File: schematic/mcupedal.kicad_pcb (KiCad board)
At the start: 2 copper layers, 33 x 87.6 mm, 23 parts, among them J1 Barrel_Jack_Switch, J2 AudioJack3_Switch, J3 Screw_Terminal_01x02, J4 AudioJack3_Switch, J5 Screw_Terminal_01x03, J6 Screw_Terminal_01x03, U1 AMS1117-3.3, U2 footswitch, U3 Opamp_Dual, U4 ATtiny85-20P

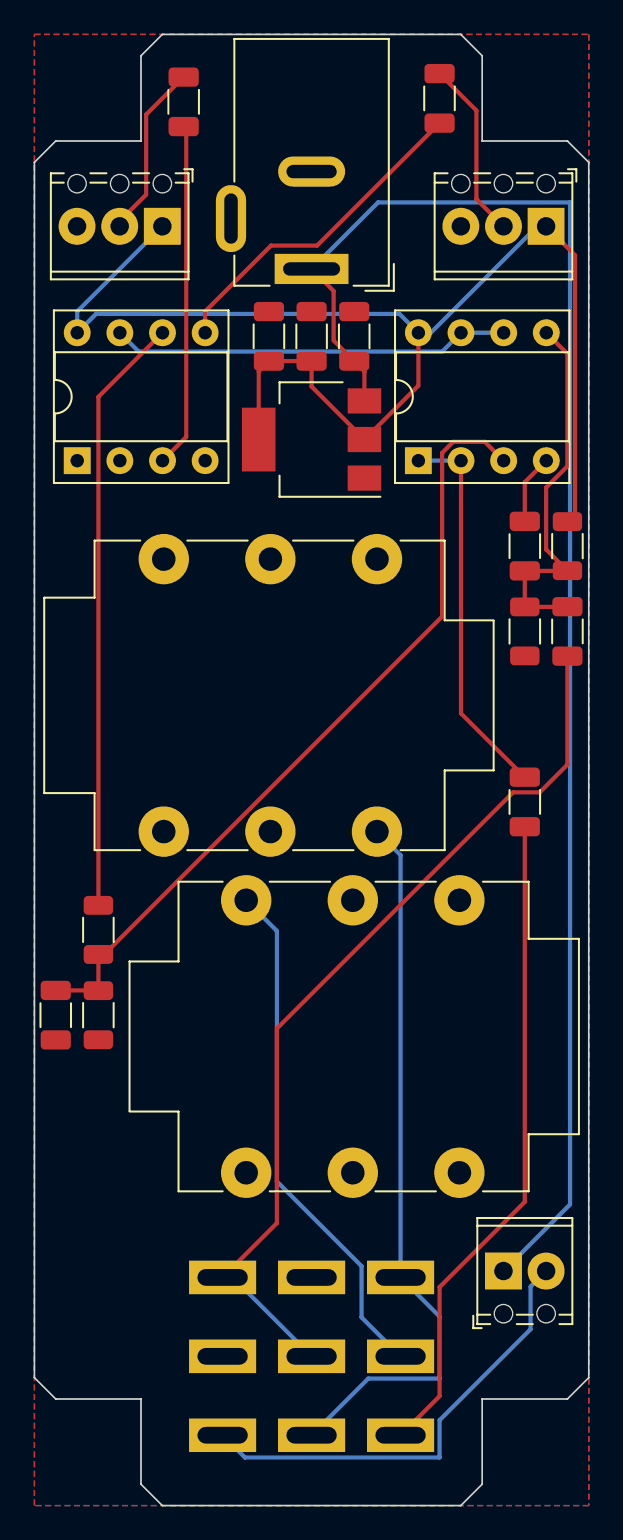
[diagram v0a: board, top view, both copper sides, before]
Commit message: feat(pcb): swap dc pins
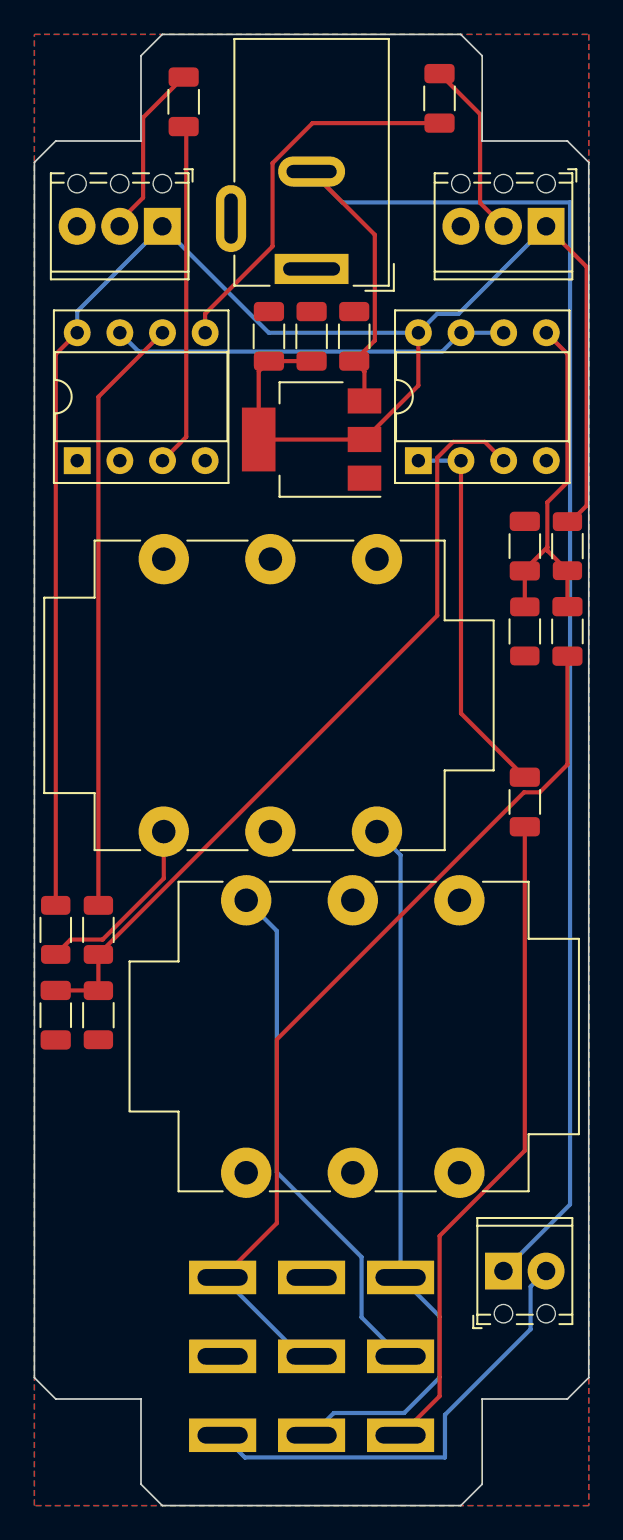
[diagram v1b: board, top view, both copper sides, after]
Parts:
- added R1: 100, Resistor_SMD:R_1206_3216Metric, F.Cu at (26.7, 78.7)
- renumbered R1 to R2, R2 to R3, R3 to R4, R4 to R5
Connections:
- J1 pad 1: +9V -> GND
- J1 pad 2: GND -> +9V
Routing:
- net +3V3: track 79.5 -> 111.8 mm
- net GND: track 4.15 -> 11.1 mm
- net +9V: track 91.5 -> 97.4 mm
- net Net-(C9-Pad1): track 19.9 -> 22.7 mm
- net Net-(C5-Pad1): track 23.0 -> 21.9 mm

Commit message: feat(schematic): cleanup
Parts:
- R3: value 200K -> 220K
- moved J4 9.46 mm to (45.8, 71.6), turned to 180 degrees
- moved J2 8.28 mm to (38.0, 75.7), turned to 0 degrees
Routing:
- net Net-(J4-PadT): track 31.0 -> 35.0 mm
- net Net-(J2-PadT): track 43.1 -> 39.1 mm
- net Net-(U2-Pad1): track 53.3 -> 54.4 mm
- net +9V: track 97.4 -> 98.5 mm
- net GND: track 11.1 -> 12.1 mm
- net Net-(R4-Pad1): track 35.7 -> 36.2 mm
- net Net-(C5-Pad1): track 21.9 -> 22.5 mm

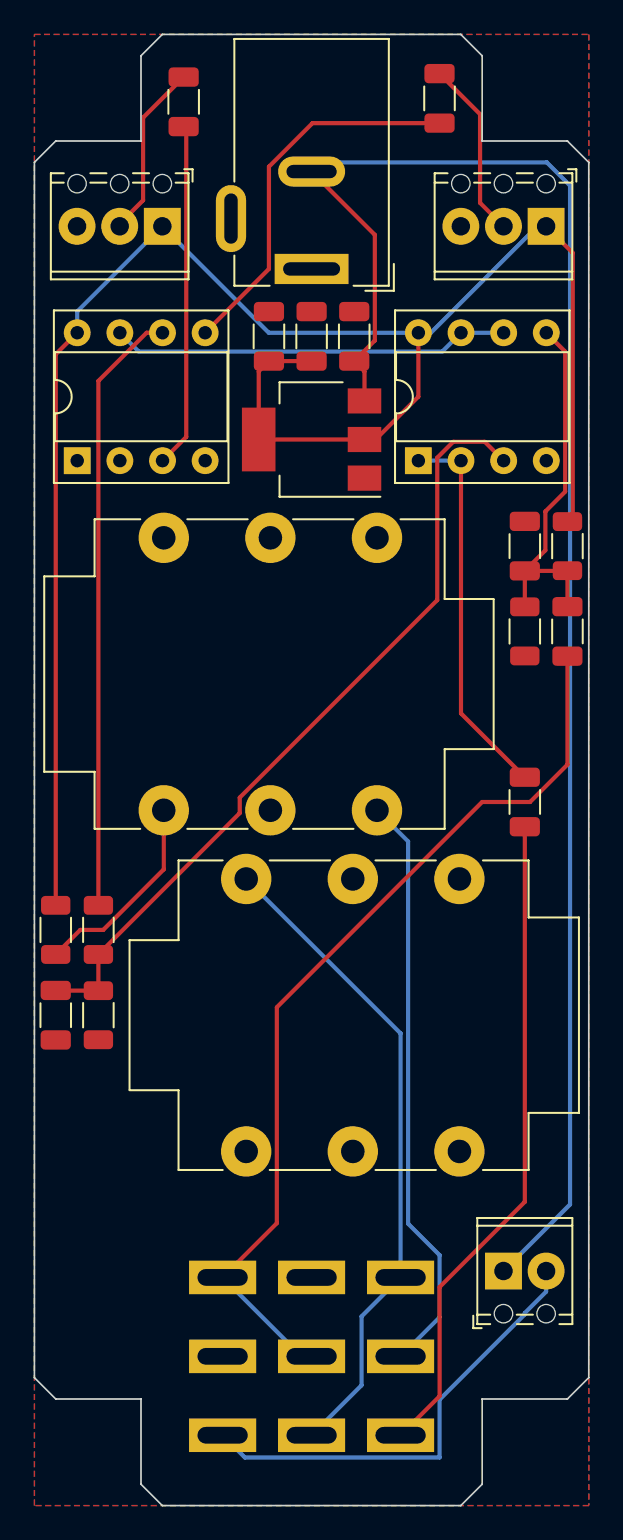
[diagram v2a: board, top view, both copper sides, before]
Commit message: chore(tidy): removed unused components
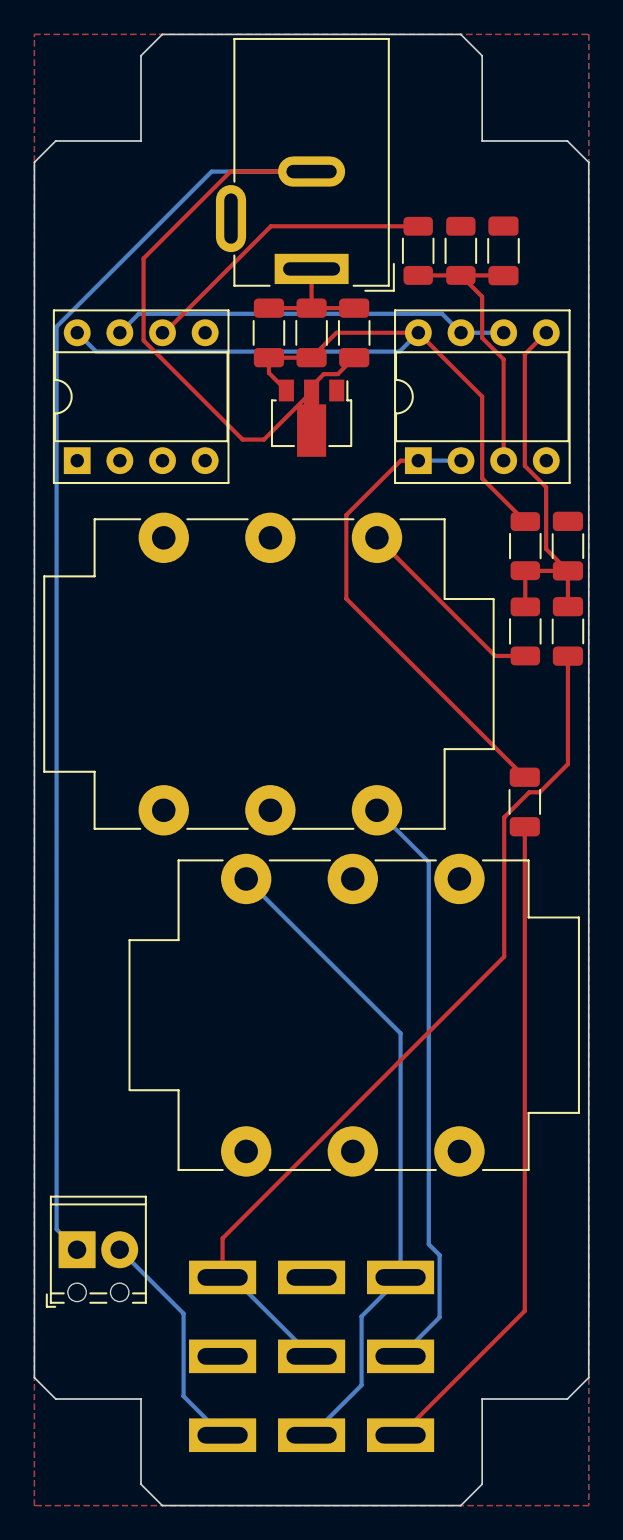
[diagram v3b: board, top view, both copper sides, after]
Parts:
- removed C8, C9: 100nF, Capacitor_SMD:C_1206_3216Metric
- removed J5, J6: Screw_Terminal_01x03, TerminalBlock_Phoenix:TerminalBlock_Phoenix_MPT-0,5-3-2.54_1x03_P2.54mm_Horizontal
- removed R5: 47K, Resistor_SMD:R_1206_3216Metric
- C6: value 100nF -> 220pF
- C7: value 220pF -> 100nF
- R1: value 100 -> 1M
- R2: value 1M -> 220K
- R3: value 220K -> 100K
- R4: value 100K -> 47K
- U1: value AMS1117-3.3 -> HT75xx-1-SOT89; footprint Package_TO_SOT_SMD:SOT-223-3_TabPin2 -> Package_TO_SOT_SMD:SOT-89-3
- moved R4 45.8 mm to (50.8, 38.3), turned to 90 degrees
- moved R1 36.1 mm to (54.6, 55.9)
- moved C7 30.7 mm to (54.6, 71.1)
- moved J3 25.4 mm to (27.9, 97.8)
- moved R3 23.5 mm to (48.3, 38.3)
- moved C6 21.0 mm to (53.3, 38.3)
- moved R2 5.67 mm to (54.6, 61.0)
- moved C5 2.57 mm to (57.2, 55.9)
- moved U1 1.27 mm to (41.9, 48.3), turned to -90 degrees
- moved C1 0.20 mm to (44.5, 43.2)
- moved C2 0.20 mm to (41.9, 43.2)
- moved C3 0.20 mm to (39.4, 43.2)
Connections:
- C4 pad 2: Net-(C5-Pad1) -> Net-(C4-Pad2)
- C5 pad 1: Net-(C5-Pad1) -> Net-(C4-Pad2)
- C6 pad 2: Net-(C6-Pad2) -> GND
- C7 pad 2: GND -> Net-(C7-Pad2)
- R1 pad 2: GND -> Net-(C4-Pad2)
- R2 pad 1: +3V3 -> Net-(C4-Pad2)
- R2 pad 2: Net-(C5-Pad1) -> GND
- R3 pad 1: Net-(C5-Pad1) -> Net-(R3-Pad1)
- R3 pad 2: GND -> Net-(C6-Pad1)
- R4 pad 1: Net-(R4-Pad1) -> Net-(C6-Pad1)
- R4 pad 2: Net-(C7-Pad1) -> GND
- U1 pad 2: +3V3 -> +9V
- U1 pad 3: +9V -> +3V3
- U2 pad 9: Net-(C8-Pad2) -> Net-(C7-Pad2)
- U3 pad 1: Net-(C8-Pad1) -> Net-(C7-Pad1)
- U3 pad 2: Net-(C8-Pad1) -> Net-(C7-Pad1)
- U3 pad 3: Net-(C7-Pad1) -> Net-(C6-Pad1)
- U3 pad 5: Net-(C5-Pad1) -> Net-(C4-Pad2)
- U4 pad 3: Net-(C6-Pad1) -> unconnected-(U4-Pad3)
- U4 pad 5: Net-(C9-Pad1) -> unconnected-(U4-Pad5)
- U4 pad 6: Net-(R4-Pad1) -> Net-(R3-Pad1)
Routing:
- net +3V3: track 111.4 -> 47.0 mm
- net Net-(C8-Pad2): track 39.3 -> 0.00 mm
- net Net-(C7-Pad2): track 0.00 -> 39.3 mm
- net Net-(R4-Pad1): track 36.2 -> 0.00 mm
- net Net-(C8-Pad1): track 23.0 -> 0.00 mm
- net Net-(C9-Pad1): track 22.7 -> 0.00 mm
- net Net-(C4-Pad2): track 0.00 -> 22.6 mm
- net Net-(C5-Pad1): track 22.5 -> 0.00 mm
- net Net-(C7-Pad1): track 47.5 -> 28.2 mm
- net Net-(R3-Pad1): track 0.00 -> 17.9 mm
- net Net-(J3-Pad2): track 27.2 -> 13.6 mm
- net Net-(C9-Pad2): track 10.7 -> 0.00 mm
- net Net-(C6-Pad2): track 10.5 -> 0.00 mm
- net +9V: track 98.5 -> 108.7 mm
- net GND: track 12.1 -> 19.2 mm
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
